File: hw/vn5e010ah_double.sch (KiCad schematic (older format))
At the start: 4 parts

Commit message: drawing new version of esb, not finished
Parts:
- removed R?: 390, yageo:0603, symbol yageo:390
- added D1301: DIODE_RS07J-GS18, usevolt:DO219AB, symbol usevolt:DIODE_RS07J-GS18
- added R1303: 1K, yageo:0603, symbol yageo:1K
- gave numbers to parts that had none: 3
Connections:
- net labels added: +3V3
- wire segments 36 -> 38
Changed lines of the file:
@@
 $Descr A4 11693 8268
 encoding utf-8
-Sheet 14 14
+Sheet 13 13
 Title ""
 Date ""
@@
 	5200 4100 5450 4100
 $Comp
-L power:VDD #PWR?
+L power:VDD #PWR0108
 U 1 1 5B1A4079
 P 5450 3300
-F 0 "#PWR?" H 5450 3150 50  0001 C CNN
+F 0 "#PWR0108" H 5450 3150 50  0001 C CNN
 F 1 "VDD" H 5467 3473 50  0000 C CNN
 F 2 "" H 5450 3300 50  0000 C CNN
@@
 Connection ~ 5450 3600
 $Comp
-L power:GND #PWR?
+L power:GND #PWR0109
 U 1 1 5B1A4087
 P 4700 3900
-F 0 "#PWR?" H 4700 3650 50  0001 C CNN
+F 0 "#PWR0109" H 4700 3650 50  0001 C CNN
 F 1 "GND" H 4705 3727 50  0000 C CNN
 F 2 "" H 4700 3900 50  0000 C CNN
@@
 AR Path="/5A13680F/5B1A4092" Ref="R?"  Part="1"
 AR Path="/5A14370A/5B1A4092" Ref="R?"  Part="1"
-F 0 "R?" V 4458 3708 45  0000 L CNN
+AR Path="/5B1A3D6E/5B1A4092" Ref="R1302"  Part="1"
+F 0 "R1302" V 4458 3708 45  0000 L CNN
 F 1 "1K" V 4542 3708 45  0000 L CNN
 F 2 "yageo:0603" H 4480 3800 20  0001 C CNN
@@
 Connection ~ 4700 3850
 $Comp
-L yageo:390 R?
-U 1 1 5B1A40A1
-P 5000 3600
-AR Path="/5A1349CF/5B1A40A1" Ref="R?"  Part="1"
-AR Path="/5A14370A/5B1A40A1" Ref="R?"  Part="1"
-AR Path="/5A120DD2/5B1A40A1" Ref="R?"  Part="1"
-AR Path="/5A12FF64/5B1A40A1" Ref="R?"  Part="1"
-AR Path="/5A130D3E/5B1A40A1" Ref="R?"  Part="1"
-AR Path="/5A1358B0/5B1A40A1" Ref="R?"  Part="1"
-AR Path="/5A13680F/5B1A40A1" Ref="R?"  Part="1"
-F 0 "R?" H 5050 3784 45  0000 C CNN
-F 1 "390" H 5050 3700 45  0000 C CNN
-F 2 "yageo:0603" H 5030 3750 20  0001 C CNN
-F 3 "" H 4969 3639 60  0001 C CNN
-F 4 "" H 5369 4039 60  0001 C CNN "1st Source Part Number"
-F 5 "Digikey" H 5269 3939 60  0001 C CNN "1st Source"
-F 6 "RC0603FR-07390RL" H 5169 3839 60  0001 C CNN "Manufacturer Part Number"
-F 7 "YAGEO" H 5069 3739 60  0001 C CNN "Manufacturer"
-	1    5000 3600
-	1    0    0    -1
-$EndComp
-$Comp
-L usevolt:VN5E010AH U?
+L usevolt:VN5E010AH U1303
 U 1 1 5B1A40AC
 P 6700 3600
-F 0 "U?" H 6650 4047 60  0000 C CNN
+F 0 "U1303" H 6650 4047 60  0000 C CNN
 F 1 "VN5E010AH" H 6650 3941 60  0000 C CNN
 F 2 "usevolt:HPAK" H 6350 4550 60  0001 C CNN
@@
 $EndComp
 $Comp
-L power:GND #PWR?
+L power:GND #PWR0110
 U 1 1 5B1A40B3
 P 5650 3900
-F 0 "#PWR?" H 5650 3650 50  0001 C CNN
+F 0 "#PWR0110" H 5650 3650 50  0001 C CNN
 F 1 "GND" H 5655 3727 50  0000 C CNN
 F 2 "" H 5650 3900 50  0000 C CNN
@@
 	5650 3800 5650 3900
 $Comp
-L usevolt:VN5E010AH U?
+L usevolt:VN5E010AH U1302
 U 1 1 5B1A4293
 P 6700 2800
-F 0 "U?" H 6650 3247 60  0000 C CNN
+F 0 "U1302" H 6650 3247 60  0000 C CNN
 F 1 "VN5E010AH" H 6650 3141 60  0000 C CNN
 F 2 "usevolt:HPAK" H 6350 3750 60  0001 C CNN
@@
 	6150 2900 6150 3000
 Connection ~ 6150 3000
+$Comp
+L yageo:1K R1303
+U 1 1 5B2322BF
+P 5000 3600
+F 0 "R1303" H 5050 3784 45  0000 C CNN
+F 1 "1K" H 5050 3700 45  0000 C CNN
+F 2 "yageo:0603" H 5030 3750 20  0001 C CNN
+F 3 "" H 4969 3639 60  0001 C CNN
+F 4 "" H 5369 4039 60  0001 C CNN "1st Source Part Number"
+F 5 "Digikey" H 5269 3939 60  0001 C CNN "1st Source"
+F 6 "RC0603FR-071KL" H 5169 3839 60  0001 C CNN "Manufacturer Part Number"
+F 7 "YAGEO" H 5069 3739 60  0001 C CNN "Manufacturer"
+	1    5000 3600
+	1    0    0    -1
+$EndComp
+$Comp
+L usevolt:DIODE_RS07J-GS18 D1301
+U 1 1 5B2324C2
+P 5250 4400
+F 0 "D1301" H 5200 4260 45  0000 C CNN
+F 1 "DIODE_RS07J-GS18" H 5270 4340 45  0001 L BNN
+F 2 "usevolt:DO219AB" H 5280 4550 20  0001 C CNN
+F 3 "http://www.vishay.com/docs/85742/rs07b.pdf" H 5270 4420 60  0001 C CNN
+F 4 "1864882" H 5870 5020 60  0001 C CNN "2nd Source Part Number"
+F 5 "Digi-Key" H 5570 4720 60  0001 C CNN "1st Source"
+F 6 "Farnell" H 5770 4920 60  0001 C CNN "2nd Source"
+F 7 "RS07J-GS18" H 5470 4620 60  0001 C CNN "Manufacturer Part Number"
+F 8 "RS07J-GS18-ND" H 5670 4820 60  0001 C CNN "1st Source Part Number"
+F 9 "Vishay Semiconductor Diodes Division" H 5370 4520 60  0001 C CNN "Manufacturer"
+	1    5250 4400
+	-1   0    0    1
+$EndComp
+$Comp
+L power:+3V3 #PWR0111
+U 1 1 5B2325C0
+P 4950 4400
+F 0 "#PWR0111" H 4950 4250 50  0001 C CNN
+F 1 "+3V3" H 4965 4573 50  0000 C CNN
+F 2 "" H 4950 4400 50  0000 C CNN
+F 3 "" H 4950 4400 50  0000 C CNN
+	1    4950 4400
+	1    0    0    -1
+$EndComp
+Wire Wire Line
+	4950 4400 5150 4400
+Wire Wire Line
+	5450 4400 5450 4100
+Connection ~ 5450 4100
 $EndSCHEMATC

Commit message: hw version 5.0.0, for hcu enclosure
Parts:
- renumbered D1301 to D1201, R1302 to R1101, R1303 to R1203, U1302 to U1201, U1303 to U1202
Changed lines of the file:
@@
 $Descr A4 11693 8268
 encoding utf-8
-Sheet 13 13
+Sheet 12 12
 Title ""
 Date ""
@@
 	5200 4100 5450 4100
 $Comp
-L power:VDD #PWR0108
+L power:VDD #PWR01203
 U 1 1 5B1A4079
 P 5450 3300
-F 0 "#PWR0108" H 5450 3150 50  0001 C CNN
+AR Path="/5B1A3D6E/5B1A4079" Ref="#PWR01203"  Part="1"
+AR Path="/5A13680F/5B1A4079" Ref="#PWR01103"  Part="1"
+F 0 "#PWR01203" H 5450 3150 50  0001 C CNN
 F 1 "VDD" H 5467 3473 50  0000 C CNN
 F 2 "" H 5450 3300 50  0000 C CNN
@@
 Connection ~ 5450 3600
 $Comp
-L power:GND #PWR0109
+L power:GND #PWR01201
 U 1 1 5B1A4087
 P 4700 3900
-F 0 "#PWR0109" H 4700 3650 50  0001 C CNN
+AR Path="/5B1A3D6E/5B1A4087" Ref="#PWR01201"  Part="1"
+AR Path="/5A13680F/5B1A4087" Ref="#PWR01101"  Part="1"
+F 0 "#PWR01201" H 4700 3650 50  0001 C CNN
 F 1 "GND" H 4705 3727 50  0000 C CNN
 F 2 "" H 4700 3900 50  0000 C CNN
@@
 AR Path="/5A1349CF/5B1A4092" Ref="R?"  Part="1"
 AR Path="/5A1358B0/5B1A4092" Ref="R?"  Part="1"
-AR Path="/5A13680F/5B1A4092" Ref="R?"  Part="1"
+AR Path="/5A13680F/5B1A4092" Ref="R1101"  Part="1"
 AR Path="/5A14370A/5B1A4092" Ref="R?"  Part="1"
-AR Path="/5B1A3D6E/5B1A4092" Ref="R1302"  Part="1"
-F 0 "R1302" V 4458 3708 45  0000 L CNN
+AR Path="/5B1A3D6E/5B1A4092" Ref="R1202"  Part="1"
+F 0 "R1202" V 4458 3708 45  0000 L CNN
 F 1 "1K" V 4542 3708 45  0000 L CNN
 F 2 "yageo:0603" H 4480 3800 20  0001 C CNN
@@
 Connection ~ 4700 3850
 $Comp
-L usevolt:VN5E010AH U1303
+L usevolt:VN5E010AH U1202
 U 1 1 5B1A40AC
 P 6700 3600
-F 0 "U1303" H 6650 4047 60  0000 C CNN
+AR Path="/5B1A3D6E/5B1A40AC" Ref="U1202"  Part="1"
+AR Path="/5A13680F/5B1A40AC" Ref="U1103"  Part="1"
+F 0 "U1202" H 6650 4047 60  0000 C CNN
 F 1 "VN5E010AH" H 6650 3941 60  0000 C CNN
 F 2 "usevolt:HPAK" H 6350 4550 60  0001 C CNN
@@
 $EndComp
 $Comp
-L power:GND #PWR0110
+L power:GND #PWR01204
 U 1 1 5B1A40B3
 P 5650 3900
-F 0 "#PWR0110" H 5650 3650 50  0001 C CNN
+AR Path="/5B1A3D6E/5B1A40B3" Ref="#PWR01204"  Part="1"
+AR Path="/5A13680F/5B1A40B3" Ref="#PWR01104"  Part="1"
+F 0 "#PWR01204" H 5650 3650 50  0001 C CNN
 F 1 "GND" H 5655 3727 50  0000 C CNN
 F 2 "" H 5650 3900 50  0000 C CNN
@@
 	5650 3800 5650 3900
 $Comp
-L usevolt:VN5E010AH U1302
+L usevolt:VN5E010AH U1201
 U 1 1 5B1A4293
 P 6700 2800
-F 0 "U1302" H 6650 3247 60  0000 C CNN
+AR Path="/5B1A3D6E/5B1A4293" Ref="U1201"  Part="1"
+AR Path="/5A13680F/5B1A4293" Ref="U1102"  Part="1"
+F 0 "U1201" H 6650 3247 60  0000 C CNN
 F 1 "VN5E010AH" H 6650 3141 60  0000 C CNN
 F 2 "usevolt:HPAK" H 6350 3750 60  0001 C CNN
@@
 Connection ~ 6150 3000
 $Comp
-L yageo:1K R1303
+L yageo:1K R1203
 U 1 1 5B2322BF
 P 5000 3600
-F 0 "R1303" H 5050 3784 45  0000 C CNN
+AR Path="/5B1A3D6E/5B2322BF" Ref="R1203"  Part="1"
+AR Path="/5A13680F/5B2322BF" Ref="R1102"  Part="1"
+F 0 "R1203" H 5050 3784 45  0000 C CNN
 F 1 "1K" H 5050 3700 45  0000 C CNN
 F 2 "yageo:0603" H 5030 3750 20  0001 C CNN
@@
 $EndComp
 $Comp
-L usevolt:DIODE_RS07J-GS18 D1301
+L usevolt:DIODE_RS07J-GS18 D1201
 U 1 1 5B2324C2
 P 5250 4400
-F 0 "D1301" H 5200 4260 45  0000 C CNN
+AR Path="/5B1A3D6E/5B2324C2" Ref="D1201"  Part="1"
+AR Path="/5A13680F/5B2324C2" Ref="D1101"  Part="1"
+F 0 "D1201" H 5200 4260 45  0000 C CNN
 F 1 "DIODE_RS07J-GS18" H 5270 4340 45  0001 L BNN
 F 2 "usevolt:DO219AB" H 5280 4550 20  0001 C CNN
@@
 $EndComp
 $Comp
-L power:+3V3 #PWR0111
+L power:+3V3 #PWR01202
 U 1 1 5B2325C0
 P 4950 4400
-F 0 "#PWR0111" H 4950 4250 50  0001 C CNN
+AR Path="/5B1A3D6E/5B2325C0" Ref="#PWR01202"  Part="1"
+AR Path="/5A13680F/5B2325C0" Ref="#PWR01102"  Part="1"
+F 0 "#PWR01202" H 4950 4250 50  0001 C CNN
 F 1 "+3V3" H 4965 4573 50  0000 C CNN
 F 2 "" H 4950 4400 50  0000 C CNN

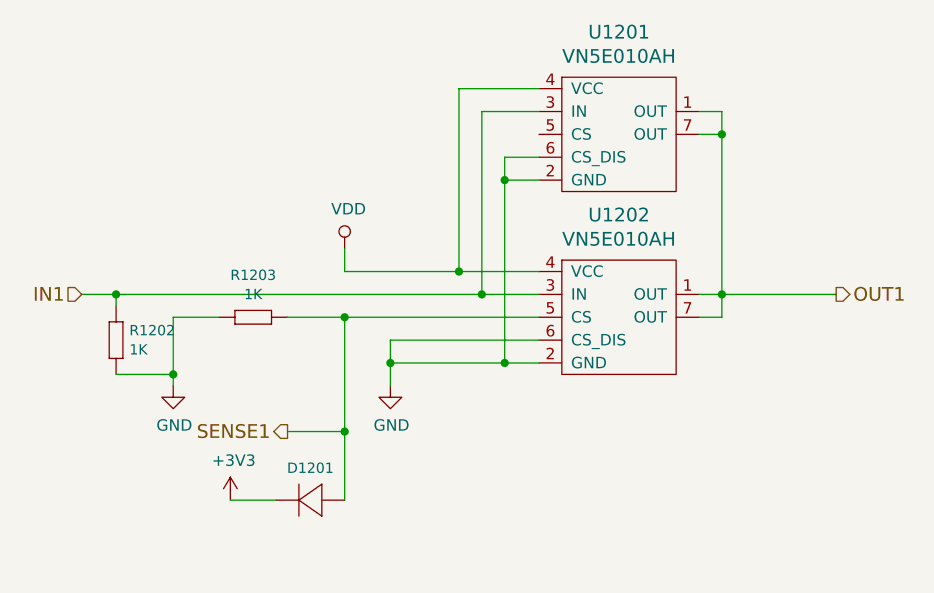
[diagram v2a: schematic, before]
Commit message: pulldown resistors added to power outputs
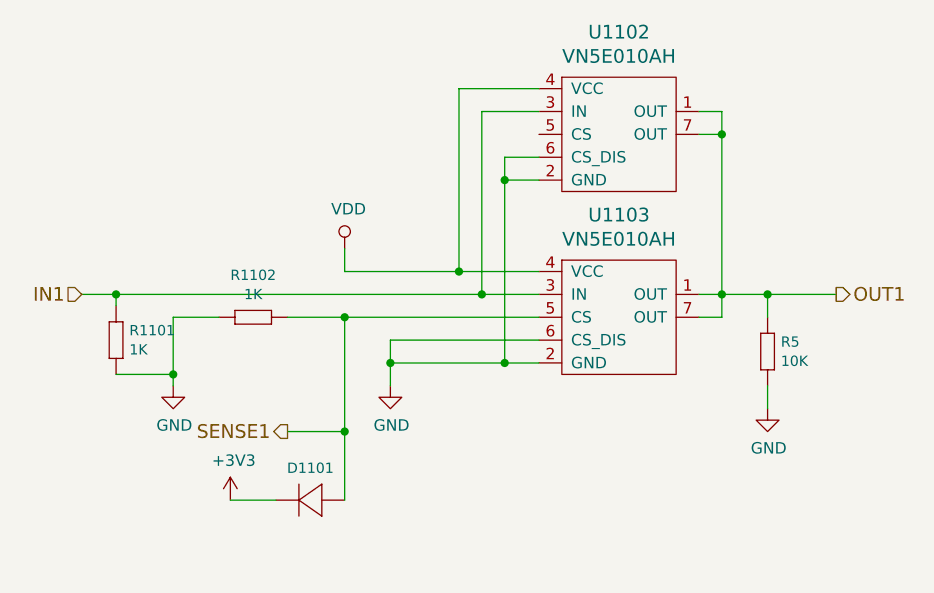
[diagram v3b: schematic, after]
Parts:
- added R6: 10K, yageo:0603, symbol yageo:10K
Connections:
- net GND: now also R6.1 (R1)
- net OUT1: now also R6.2 (R2)
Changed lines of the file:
@@
 AR Path="/5B1A3D6E/5B1A4079" Ref="#PWR01203"  Part="1"
 AR Path="/5A13680F/5B1A4079" Ref="#PWR01103"  Part="1"
-F 0 "#PWR01203" H 5450 3150 50  0001 C CNN
+F 0 "#PWR01103" H 5450 3150 50  0001 C CNN
 F 1 "VDD" H 5467 3473 50  0000 C CNN
 F 2 "" H 5450 3300 50  0000 C CNN
@@
 AR Path="/5B1A3D6E/5B1A4087" Ref="#PWR01201"  Part="1"
 AR Path="/5A13680F/5B1A4087" Ref="#PWR01101"  Part="1"
-F 0 "#PWR01201" H 4700 3650 50  0001 C CNN
+F 0 "#PWR01101" H 4700 3650 50  0001 C CNN
 F 1 "GND" H 4705 3727 50  0000 C CNN
 F 2 "" H 4700 3900 50  0000 C CNN
@@
 AR Path="/5A14370A/5B1A4092" Ref="R?"  Part="1"
 AR Path="/5B1A3D6E/5B1A4092" Ref="R1202"  Part="1"
-F 0 "R1202" V 4458 3708 45  0000 L CNN
+F 0 "R1101" V 4458 3708 45  0000 L CNN
 F 1 "1K" V 4542 3708 45  0000 L CNN
 F 2 "yageo:0603" H 4480 3800 20  0001 C CNN
@@
 AR Path="/5B1A3D6E/5B1A40AC" Ref="U1202"  Part="1"
 AR Path="/5A13680F/5B1A40AC" Ref="U1103"  Part="1"
-F 0 "U1202" H 6650 4047 60  0000 C CNN
+F 0 "U1103" H 6650 4047 60  0000 C CNN
 F 1 "VN5E010AH" H 6650 3941 60  0000 C CNN
 F 2 "usevolt:HPAK" H 6350 4550 60  0001 C CNN
@@
 AR Path="/5B1A3D6E/5B1A40B3" Ref="#PWR01204"  Part="1"
 AR Path="/5A13680F/5B1A40B3" Ref="#PWR01104"  Part="1"
-F 0 "#PWR01204" H 5650 3650 50  0001 C CNN
+F 0 "#PWR01104" H 5650 3650 50  0001 C CNN
 F 1 "GND" H 5655 3727 50  0000 C CNN
 F 2 "" H 5650 3900 50  0000 C CNN
@@
 Connection ~ 5650 3800
 Wire Wire Line
-	7100 3500 7600 3500
+	7100 3500 7300 3500
 Wire Wire Line
 	5450 3600 6300 3600
@@
 AR Path="/5B1A3D6E/5B1A4293" Ref="U1201"  Part="1"
 AR Path="/5A13680F/5B1A4293" Ref="U1102"  Part="1"
-F 0 "U1201" H 6650 3247 60  0000 C CNN
+F 0 "U1102" H 6650 3247 60  0000 C CNN
 F 1 "VN5E010AH" H 6650 3141 60  0000 C CNN
 F 2 "usevolt:HPAK" H 6350 3750 60  0001 C CNN
@@
 AR Path="/5B1A3D6E/5B2322BF" Ref="R1203"  Part="1"
 AR Path="/5A13680F/5B2322BF" Ref="R1102"  Part="1"
-F 0 "R1203" H 5050 3784 45  0000 C CNN
+F 0 "R1102" H 5050 3784 45  0000 C CNN
 F 1 "1K" H 5050 3700 45  0000 C CNN
 F 2 "yageo:0603" H 5030 3750 20  0001 C CNN
@@
 AR Path="/5B1A3D6E/5B2324C2" Ref="D1201"  Part="1"
 AR Path="/5A13680F/5B2324C2" Ref="D1101"  Part="1"
-F 0 "D1201" H 5200 4260 45  0000 C CNN
+F 0 "D1101" H 5200 4260 45  0000 C CNN
 F 1 "DIODE_RS07J-GS18" H 5270 4340 45  0001 L BNN
 F 2 "usevolt:DO219AB" H 5280 4550 20  0001 C CNN
@@
 AR Path="/5B1A3D6E/5B2325C0" Ref="#PWR01202"  Part="1"
 AR Path="/5A13680F/5B2325C0" Ref="#PWR01102"  Part="1"
-F 0 "#PWR01202" H 4950 4250 50  0001 C CNN
+F 0 "#PWR01102" H 4950 4250 50  0001 C CNN
 F 1 "+3V3" H 4965 4573 50  0000 C CNN
 F 2 "" H 4950 4400 50  0000 C CNN
@@
 	5450 4400 5450 4100
 Connection ~ 5450 4100
+$Comp
+L yageo:10K R6
+U 1 1 5BA96DF9
+P 7300 3700
+AR Path="/5B1A3D6E/5BA96DF9" Ref="R6"  Part="1"
+AR Path="/5A13680F/5BA96DF9" Ref="R5"  Part="1"
+F 0 "R5" V 7308 3758 45  0000 L CNN
+F 1 "10K" V 7392 3758 45  0000 L CNN
+F 2 "yageo:0603" H 7330 3850 20  0001 C CNN
+F 3 "" H 7269 3739 60  0001 C CNN
+F 4 "" H 7669 4139 60  0001 C CNN "1st Source Part Number"
+F 5 "Digikey" H 7569 4039 60  0001 C CNN "1st Source"
+F 6 "RC0603FR-0710KL" H 7469 3939 60  0001 C CNN "Manufacturer Part Number"
+F 7 "YAGEO" H 7369 3839 60  0001 C CNN "Manufacturer"
+	1    7300 3700
+	0    1    1    0
+$EndComp
+Wire Wire Line
+	7300 3600 7300 3500
+Connection ~ 7300 3500
+Wire Wire Line
+	7300 3500 7600 3500
+$Comp
+L power:GND #PWR0111
+U 1 1 5BA9746E
+P 7300 4000
+AR Path="/5B1A3D6E/5BA9746E" Ref="#PWR0111"  Part="1"
+AR Path="/5A13680F/5BA9746E" Ref="#PWR0110"  Part="1"
+F 0 "#PWR0110" H 7300 3750 50  0001 C CNN
+F 1 "GND" H 7305 3827 50  0000 C CNN
+F 2 "" H 7300 4000 50  0000 C CNN
+F 3 "" H 7300 4000 50  0000 C CNN
+	1    7300 4000
+	1    0    0    -1
+$EndComp
+Wire Wire Line
+	7300 4000 7300 3900
 $EndSCHEMATC

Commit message: sense protection diodes replaced to zeners
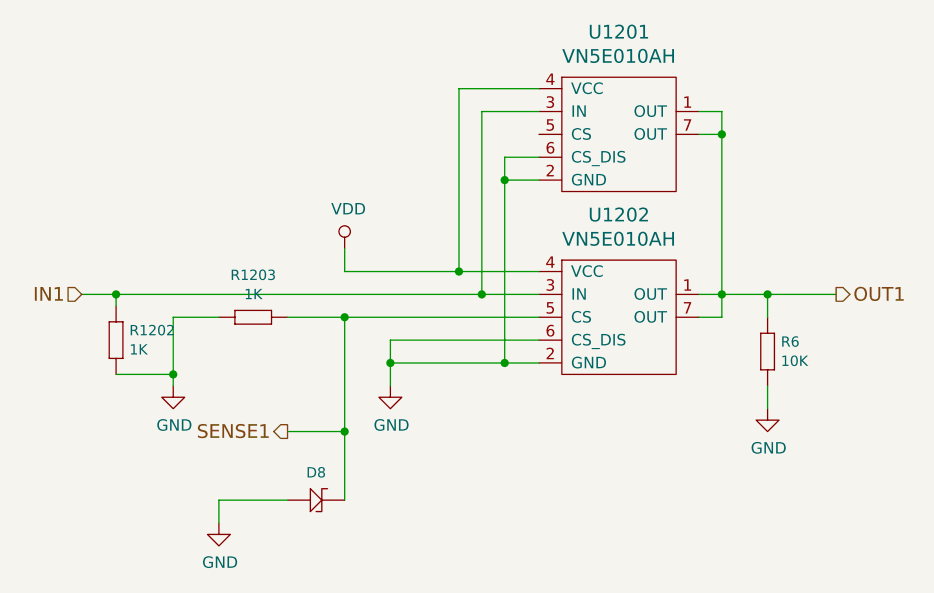
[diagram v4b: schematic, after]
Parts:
- removed D1201: DIODE_RS07J-GS18, usevolt:DO219AB, symbol usevolt:DIODE_RS07J-GS18
- added D8: ZENER_MM3Z3V6T1G, usevolt:SOD-323, symbol usevolt:ZENER_MM3Z3V6T1G
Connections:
- net GND: now also D8.2
- net SENSE1: now also D8.1
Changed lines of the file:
@@
 AR Path="/5B1A3D6E/5B1A4079" Ref="#PWR01203"  Part="1"
 AR Path="/5A13680F/5B1A4079" Ref="#PWR01103"  Part="1"
-F 0 "#PWR01103" H 5450 3150 50  0001 C CNN
+F 0 "#PWR01203" H 5450 3150 50  0001 C CNN
 F 1 "VDD" H 5467 3473 50  0000 C CNN
 F 2 "" H 5450 3300 50  0000 C CNN
@@
 AR Path="/5B1A3D6E/5B1A4087" Ref="#PWR01201"  Part="1"
 AR Path="/5A13680F/5B1A4087" Ref="#PWR01101"  Part="1"
-F 0 "#PWR01101" H 4700 3650 50  0001 C CNN
+F 0 "#PWR01201" H 4700 3650 50  0001 C CNN
 F 1 "GND" H 4705 3727 50  0000 C CNN
 F 2 "" H 4700 3900 50  0000 C CNN
@@
 AR Path="/5A14370A/5B1A4092" Ref="R?"  Part="1"
 AR Path="/5B1A3D6E/5B1A4092" Ref="R1202"  Part="1"
-F 0 "R1101" V 4458 3708 45  0000 L CNN
+F 0 "R1202" V 4458 3708 45  0000 L CNN
 F 1 "1K" V 4542 3708 45  0000 L CNN
 F 2 "yageo:0603" H 4480 3800 20  0001 C CNN
@@
 AR Path="/5B1A3D6E/5B1A40AC" Ref="U1202"  Part="1"
 AR Path="/5A13680F/5B1A40AC" Ref="U1103"  Part="1"
-F 0 "U1103" H 6650 4047 60  0000 C CNN
+F 0 "U1202" H 6650 4047 60  0000 C CNN
 F 1 "VN5E010AH" H 6650 3941 60  0000 C CNN
 F 2 "usevolt:HPAK" H 6350 4550 60  0001 C CNN
@@
 AR Path="/5B1A3D6E/5B1A40B3" Ref="#PWR01204"  Part="1"
 AR Path="/5A13680F/5B1A40B3" Ref="#PWR01104"  Part="1"
-F 0 "#PWR01104" H 5650 3650 50  0001 C CNN
+F 0 "#PWR01204" H 5650 3650 50  0001 C CNN
 F 1 "GND" H 5655 3727 50  0000 C CNN
 F 2 "" H 5650 3900 50  0000 C CNN
@@
 AR Path="/5B1A3D6E/5B1A4293" Ref="U1201"  Part="1"
 AR Path="/5A13680F/5B1A4293" Ref="U1102"  Part="1"
-F 0 "U1102" H 6650 3247 60  0000 C CNN
+F 0 "U1201" H 6650 3247 60  0000 C CNN
 F 1 "VN5E010AH" H 6650 3141 60  0000 C CNN
 F 2 "usevolt:HPAK" H 6350 3750 60  0001 C CNN
@@
 AR Path="/5B1A3D6E/5B2322BF" Ref="R1203"  Part="1"
 AR Path="/5A13680F/5B2322BF" Ref="R1102"  Part="1"
-F 0 "R1102" H 5050 3784 45  0000 C CNN
+F 0 "R1203" H 5050 3784 45  0000 C CNN
 F 1 "1K" H 5050 3700 45  0000 C CNN
 F 2 "yageo:0603" H 5030 3750 20  0001 C CNN
@@
 	1    0    0    -1
 $EndComp
-$Comp
-L usevolt:DIODE_RS07J-GS18 D1201
-U 1 1 5B2324C2
-P 5250 4400
-AR Path="/5B1A3D6E/5B2324C2" Ref="D1201"  Part="1"
-AR Path="/5A13680F/5B2324C2" Ref="D1101"  Part="1"
-F 0 "D1101" H 5200 4260 45  0000 C CNN
-F 1 "DIODE_RS07J-GS18" H 5270 4340 45  0001 L BNN
-F 2 "usevolt:DO219AB" H 5280 4550 20  0001 C CNN
-F 3 "http://www.vishay.com/docs/85742/rs07b.pdf" H 5270 4420 60  0001 C CNN
-F 4 "1864882" H 5870 5020 60  0001 C CNN "2nd Source Part Number"
-F 5 "Digi-Key" H 5570 4720 60  0001 C CNN "1st Source"
-F 6 "Farnell" H 5770 4920 60  0001 C CNN "2nd Source"
-F 7 "RS07J-GS18" H 5470 4620 60  0001 C CNN "Manufacturer Part Number"
-F 8 "RS07J-GS18-ND" H 5670 4820 60  0001 C CNN "1st Source Part Number"
-F 9 "Vishay Semiconductor Diodes Division" H 5370 4520 60  0001 C CNN "Manufacturer"
-	1    5250 4400
-	-1   0    0    1
-$EndComp
-$Comp
-L power:+3V3 #PWR01202
-U 1 1 5B2325C0
-P 4950 4400
-AR Path="/5B1A3D6E/5B2325C0" Ref="#PWR01202"  Part="1"
-AR Path="/5A13680F/5B2325C0" Ref="#PWR01102"  Part="1"
-F 0 "#PWR01102" H 4950 4250 50  0001 C CNN
-F 1 "+3V3" H 4965 4573 50  0000 C CNN
-F 2 "" H 4950 4400 50  0000 C CNN
-F 3 "" H 4950 4400 50  0000 C CNN
-	1    4950 4400
-	1    0    0    -1
-$EndComp
-Wire Wire Line
-	4950 4400 5150 4400
 Wire Wire Line
 	5450 4400 5450 4100
@@
 AR Path="/5B1A3D6E/5BA96DF9" Ref="R6"  Part="1"
 AR Path="/5A13680F/5BA96DF9" Ref="R5"  Part="1"
-F 0 "R5" V 7308 3758 45  0000 L CNN
+F 0 "R6" V 7308 3758 45  0000 L CNN
 F 1 "10K" V 7392 3758 45  0000 L CNN
 F 2 "yageo:0603" H 7330 3850 20  0001 C CNN
@@
 AR Path="/5B1A3D6E/5BA9746E" Ref="#PWR0111"  Part="1"
 AR Path="/5A13680F/5BA9746E" Ref="#PWR0110"  Part="1"
-F 0 "#PWR0110" H 7300 3750 50  0001 C CNN
+F 0 "#PWR0111" H 7300 3750 50  0001 C CNN
 F 1 "GND" H 7305 3827 50  0000 C CNN
 F 2 "" H 7300 4000 50  0000 C CNN
@@
 Wire Wire Line
 	7300 4000 7300 3900
+$Comp
+L usevolt:ZENER_MM3Z3V6T1G D8
+U 1 1 5BAAE03B
+P 5400 4400
+AR Path="/5B1A3D6E/5BAAE03B" Ref="D8"  Part="1"
+AR Path="/5A13680F/5BAAE03B" Ref="D7"  Part="1"
+F 0 "D8" H 5325 4520 45  0000 C CNN
+F 1 "ZENER_MM3Z3V6T1G" H 5675 4775 45  0001 L BNN
+F 2 "usevolt:SOD-323" H 5375 4775 20  0001 C CNN
+F 3 "http://www.mouser.com/ds/2/308/MM3Z2V4T1-D-269162.pdf" H 5750 4975 60  0001 C CNN
+F 4 "Mouser" H 5720 4720 60  0001 C CNN "1st Source"
+F 5 "MM3Z3V6T1G" H 5620 4620 60  0001 C CNN "Manufacturer Part Number"
+F 6 "863-MM3Z3V6T1G" H 5820 4820 60  0001 C CNN "1st Source Part Number"
+F 7 "ON Semiconductor" H 5675 4875 60  0001 C CNN "Manufacturer"
+	1    5400 4400
+	1    0    0    -1
+$EndComp
+$Comp
+L power:GND #PWR0103
+U 1 1 5BAAE0D6
+P 4900 4500
+AR Path="/5B1A3D6E/5BAAE0D6" Ref="#PWR0103"  Part="1"
+AR Path="/5A13680F/5BAAE0D6" Ref="#PWR0102"  Part="1"
+F 0 "#PWR0103" H 4900 4250 50  0001 C CNN
+F 1 "GND" H 4905 4327 50  0000 C CNN
+F 2 "" H 4900 4500 50  0000 C CNN
+F 3 "" H 4900 4500 50  0000 C CNN
+	1    4900 4500
+	1    0    0    -1
+$EndComp
+Wire Wire Line
+	4900 4500 4900 4400
+Wire Wire Line
+	4900 4400 5200 4400
 $EndSCHEMATC
